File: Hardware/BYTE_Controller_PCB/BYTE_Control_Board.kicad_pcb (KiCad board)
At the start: 2 copper layers, 20.8 x 40.6 mm, 11 parts, among them J1 8P8C_Shielded, Q1 2N7002, U1 SeeeduinoXIAO

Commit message: modify controller board
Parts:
- removed C1: C, Capacitor_SMD:C_0603_1608Metric
- removed D1: D_Schottky, Diode_SMD:D_SOD-123
- removed Q1: 2N7002, Package_TO_SOT_SMD:SOT-23
- removed R1, R2, R3, R4, R5, R6: R_US, Resistor_SMD:R_0603_1608Metric_Pad1.05x0.95mm_HandSolder
- removed U1: SeeeduinoXIAO, XIAO:XIAO-MOUDLE14P-2.54-21X17.8MM_Through_Hole
- added REF**: U254051N4BH806, Connectors:U254051N4BH806, F.Cu at (172.2, 105.4)
- added REF**: BL653, Controller:BL653_v5, F.Cu at (160.3, 111.7)
- J1: moved to F.Cu
- moved J1 10.5 mm to (132.1, 105.8), turned to 270 degrees
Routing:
- net Net-(C1-Pad1): track 35.4 -> 0.00 mm
- net Net-(J1-Pad6): track 23.2 -> 0.00 mm
- net Net-(J1-Pad5): track 22.2 -> 0.00 mm
- net Net-(J1-Pad4): track 16.5 -> 0.00 mm
- net Net-(J1-Pad3): track 15.2 -> 0.00 mm
- net Net-(J1-Pad2): track 8.76 -> 0.00 mm
- net Net-(D1-Pad2): track 6.73 -> 0.00 mm
- net Net-(R6-Pad1): track 3.18 -> 0.00 mm
- net Net-(Q1-Pad1): track 1.84 -> 0.00 mm
- net GND: vias 5 -> 0
- removed copper zone on F.Cu, net (none)
- removed copper zone on B.Cu, net GND
- removed copper zone on F.Cu, net GND
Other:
- board size 20.8 x 40.6 mm -> 55 x 19.3 mm

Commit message: update pcbs
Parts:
- removed REF**: U254051N4BH806, Connectors:U254051N4BH806
- removed REF**: BL653, Controller:BL653_v5
- added C1: 4.7uF, Capacitor_SMD:C_0603_1608Metric, F.Cu at (145.6, 108.2)
- added C2: 4.7uF, Capacitor_SMD:C_0603_1608Metric, F.Cu at (147.6, 104.2)
- added D1: RED, LED_SMD:LED_0805_2012Metric, B.Cu at (122.0, 113.2)
- added D2: RED, LED_SMD:LED_0805_2012Metric, B.Cu at (121.9, 107.8)
- added P1: USB_C_Plug_USB2.0, Connectors:C393939, F.Cu at (168.5, 105.8)
- added R1: 2K, Resistor_SMD:R_0603_1608Metric, B.Cu at (125.4, 113.2)
- added R2: 2K, Resistor_SMD:R_0603_1608Metric, F.Cu at (149.6, 108.2)
- added R3: 2K, Resistor_SMD:R_0603_1608Metric, F.Cu at (141.4, 109.0)
- added R4: 2K, Resistor_SMD:R_0603_1608Metric, B.Cu at (125.2, 107.8)
- added R5: 2K, Resistor_SMD:R_0603_1608Metric, F.Cu at (139.9, 109.0)
- added U1: MCP73830T-2AAI_MYY, Controller:2x2TDFN, F.Cu at (147.6, 108.0)
- added U2: BL653, Controller:BL653_v5, F.Cu at (159.0, 112.0)
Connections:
- J1 pad 1: Net-(C1-Pad1) -> Net-(J1-Pad1)
- J1 pad 7: Net-(C1-Pad1) -> Net-(J1-Pad7)
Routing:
- net /STAT: track 0.00 -> 1.26 mm, vias 0 -> 1

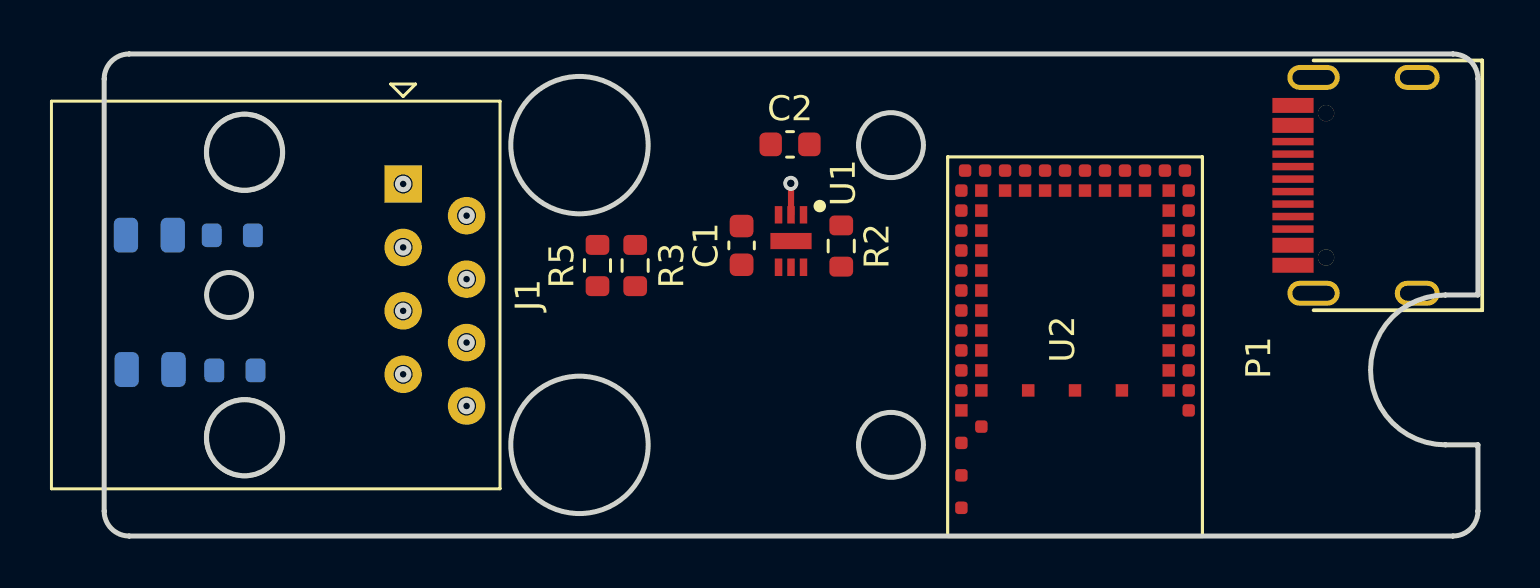
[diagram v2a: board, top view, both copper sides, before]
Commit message: update controller PCB added battery reading circuit
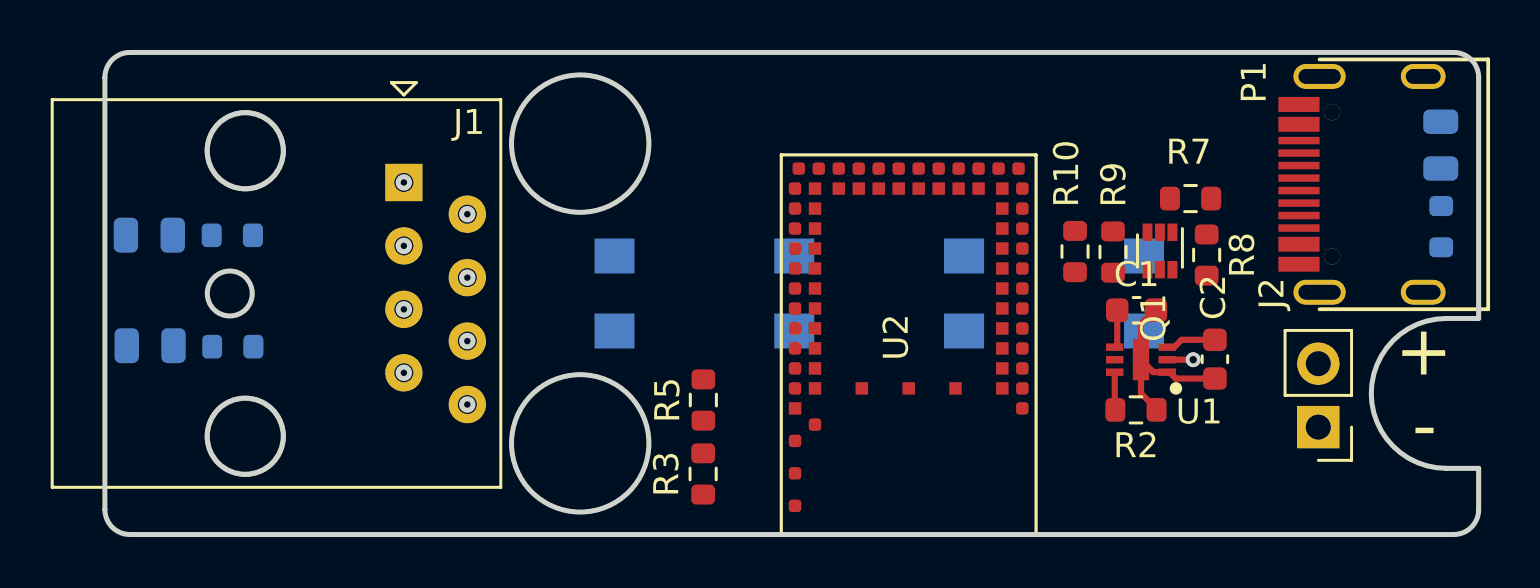
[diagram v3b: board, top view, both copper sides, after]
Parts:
- added D3: RED, LED_SMD:LED_0805_2012Metric, B.Cu at (122.0, 112.2)
- added J2: Battery, Connector_PinHeader_2.54mm:PinHeader_1x02_P2.54mm_Vertical, F.Cu at (168.7, 115.5)
- added Q1: DMC2400UV, Package_TO_SOT_SMD:SOT-563, F.Cu at (162.4, 108.5)
- added R10: 2K, Resistor_SMD:R_0603_1608Metric, F.Cu at (159.0, 108.5)
- added R6: 2K, Resistor_SMD:R_0603_1608Metric, B.Cu at (125.3, 112.3)
- added R7: 2K, Resistor_SMD:R_0603_1608Metric, F.Cu at (163.6, 106.3)
- added R8: 2K, Resistor_SMD:R_0603_1608Metric, F.Cu at (164.3, 108.6)
- added R9: 2K, Resistor_SMD:R_0603_1608Metric, F.Cu at (160.5, 108.5)
- added SW1: SW_Push, Button_Switch_SMD:SW_SPST_TL3305A, B.Cu at (144.2, 110.2)
- added SW2: SW_Push, Button_Switch_SMD:SW_SPST_TL3305A, B.Cu at (158.2, 110.2)
- moved D1 52.4 mm to (173.6, 104.2), turned to 90 degrees
- moved R1 48.6 mm to (173.7, 107.5), turned to 90 degrees
- moved C2 19.1 mm to (164.6, 112.8), turned to 270 degrees
- moved C1 16.0 mm to (161.5, 110.8), turned to 0 degrees
- moved U1 14.8 mm to (161.6, 112.8), turned to 180 degrees
- moved R2 13.5 mm to (161.4, 114.8), turned to 180 degrees
- moved R3 8.78 mm to (144.1, 117.4), turned to 270 degrees
- moved R5 6.85 mm to (144.1, 114.4)
- moved U2 6.66 mm to (152.3, 111.9)
- moved P1 0.24 mm to (168.8, 105.8)
- moved J1 0.07 mm to (132.1, 105.7)
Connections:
- R4 pad 1: /STAT -> /SIO_Z
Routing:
- net GND: track 0.00 -> 7.81 mm
- net +BATT: track 0.00 -> 2.03 mm
- net VBUS: track 0.00 -> 1.52 mm
- net Net-(R2-Pad2): track 0.00 -> 1.52 mm
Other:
- outline, holes or cut-outs redrawn
- board text added: "+"
- board text added: "-"

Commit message: update byte controller
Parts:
- added C3: 4.7uF, Capacitor_SMD:C_0603_1608Metric, F.Cu at (147.6, 103.7)
- added C4: 100nF, Capacitor_SMD:C_0603_1608Metric, F.Cu at (150.7, 103.7)
- added J3: Expansion, Connector_PinHeader_2.54mm:PinHeader_2x03_P2.54mm_Vertical, F.Cu at (138.2, 107.7)
- added J4: SWD, Connector_PinHeader_2.54mm:PinHeader_1x04_P2.54mm_Vertical, B.Cu at (127.2, 118.6)
- added R11: 5.1K, Resistor_SMD:R_0603_1608Metric, B.Cu at (170.5, 104.0)
- added R12: 5.1k, Resistor_SMD:R_0603_1608Metric, B.Cu at (171.9, 104.0)
- added R13: 10K, Resistor_SMD:R_0603_1608Metric, F.Cu at (145.6, 113.7)
- added REF**: OSHW-Logo2_7.3x6mm_SilkScreen, Symbol:OSHW-Logo2_7.3x6mm_SilkScreen, F.Cu at (143.7, 103.2)
- added Ref**: Val**, BYTE_Sensors:Logo, F.Cu at (155.5, 103.6)
- added SW3: RST, Button_Switch_SMD:SW_Push_1P1T-SH_NO_CK_KMR2xxG, F.Cu at (143.7, 117.6)
- SW1, SW2: value SW_Push -> GPIO
- moved D3 7.95 mm to (128.5, 107.7), turned to 0 degrees
- moved D2 7.88 mm to (128.5, 112.1), turned to 0 degrees
- moved R3 5.95 mm to (144.8, 111.5)
- moved R5 5.95 mm to (144.9, 108.5)
- moved R6 4.61 mm to (125.2, 107.7)
- moved R4 4.31 mm to (125.2, 112.1), turned to 0 degrees
- moved J2 0.57 mm to (169.2, 115.2)
- turned SW1 to 270 degrees
- turned SW2 to 270 degrees
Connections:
- J1 pad 2: Net-(J1-Pad2) -> /BYTE_SENSOR_1
- J1 pad 3: Net-(J1-Pad3) -> /SDA
- J1 pad 4: Net-(J1-Pad4) -> /SCL
- J1 pad 5: Net-(J1-Pad5) -> +BATT
- J1 pad 6: Net-(J1-Pad6) -> /Sensor_INT
- J1 pad 7: Net-(J1-Pad7) -> GND
- J1 pad 8: Net-(J1-Pad8) -> /BYTE_SENSOR_2
- Q1 pad 2: Net-(Q1-Pad2) -> /BATT_LVL_EN
- R10 pad 2: Net-(R10-Pad2) -> /BATT_LVL
- R4 pad 1: /SIO_Z -> /SIO_1
- R6 pad 1: /SIO_W -> /SIO_5
- R7 pad 2: Net-(Q1-Pad2) -> /BATT_LVL_EN
- R9 pad 1: Net-(R10-Pad2) -> /BATT_LVL
- SW1 pad 1: /SIO_X -> /SIO_20
- SW2 pad 1: /SIO_Y -> /SIO_0
- U2 pad 10: Net-(U2-Pad10) -> /SIO_24
- U2 pad 13: Net-(U2-Pad13) -> /SIO_20
- U2 pad 16: Net-(U2-Pad16) -> /BYTE_SENSOR_1
- U2 pad 18: Net-(U2-Pad18) -> /BYTE_SENSOR_2
- U2 pad 19: Net-(U2-Pad19) -> /RST
- U2 pad 24: Net-(U2-Pad24) -> VBUS
- U2 pad 25: Net-(U2-Pad25) -> +BATT
- U2 pad 37: Net-(U2-Pad37) -> /Sensor_INT
- U2 pad 39: Net-(U2-Pad39) -> /SIO_5
- U2 pad 41: Net-(U2-Pad41) -> /SIO_1
- U2 pad 42: Net-(U2-Pad42) -> /SIO_0
- U2 pad 45: Net-(U2-Pad45) -> /BATT_LVL_EN
- U2 pad 49: Net-(U2-Pad49) -> /BATT_LVL
- U2 pad 5: Net-(U2-Pad5) -> /SCL
- U2 pad 7: Net-(U2-Pad7) -> /SDA
- U2 pad 8: Net-(U2-Pad8) -> /SIO_25
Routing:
- net +BATT: track 2.03 -> 115.1 mm, vias 0 -> 3
- net VBUS: track 1.52 -> 62.5 mm, vias 0 -> 5
- net /SIO_1: track 0.00 -> 49.9 mm, vias 0 -> 1
- net GND: track 7.81 -> 55.4 mm, vias 0 -> 15
- net /Sensor_INT: track 0.00 -> 45.5 mm, vias 0 -> 2
- net /SIO_5: track 0.00 -> 42.8 mm, vias 0 -> 1
- net /BYTE_SENSOR_1: track 0.00 -> 39.2 mm, vias 0 -> 1
- net /D-: track 0.00 -> 38.1 mm
- net /D+: track 0.00 -> 38.1 mm
- net /BYTE_SENSOR_2: track 0.00 -> 35.8 mm, vias 0 -> 1
- net /SIO_25: track 0.00 -> 31.4 mm, vias 0 -> 1
- net /SIO_24: track 0.00 -> 30.7 mm, vias 0 -> 1
- net /SWCLK: track 0.00 -> 24.5 mm
- net /SWDIO: track 0.00 -> 22.8 mm
- net /RST: track 0.00 -> 19.4 mm, vias 0 -> 2
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- added copper zone on B.Cu, net GND
- added copper zone on F.Cu, net GND
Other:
- outline, holes or cut-outs redrawn
- net class Default: trace_width 0.25 -> 0.2
- board text added: "BYTE Controller"
- board text added: "CLK"
- board text added: "Controller"
- board text added: "DIO"
- board text added: "GND"
- board text added: "Vbatt"
- board text added: "v1.0"

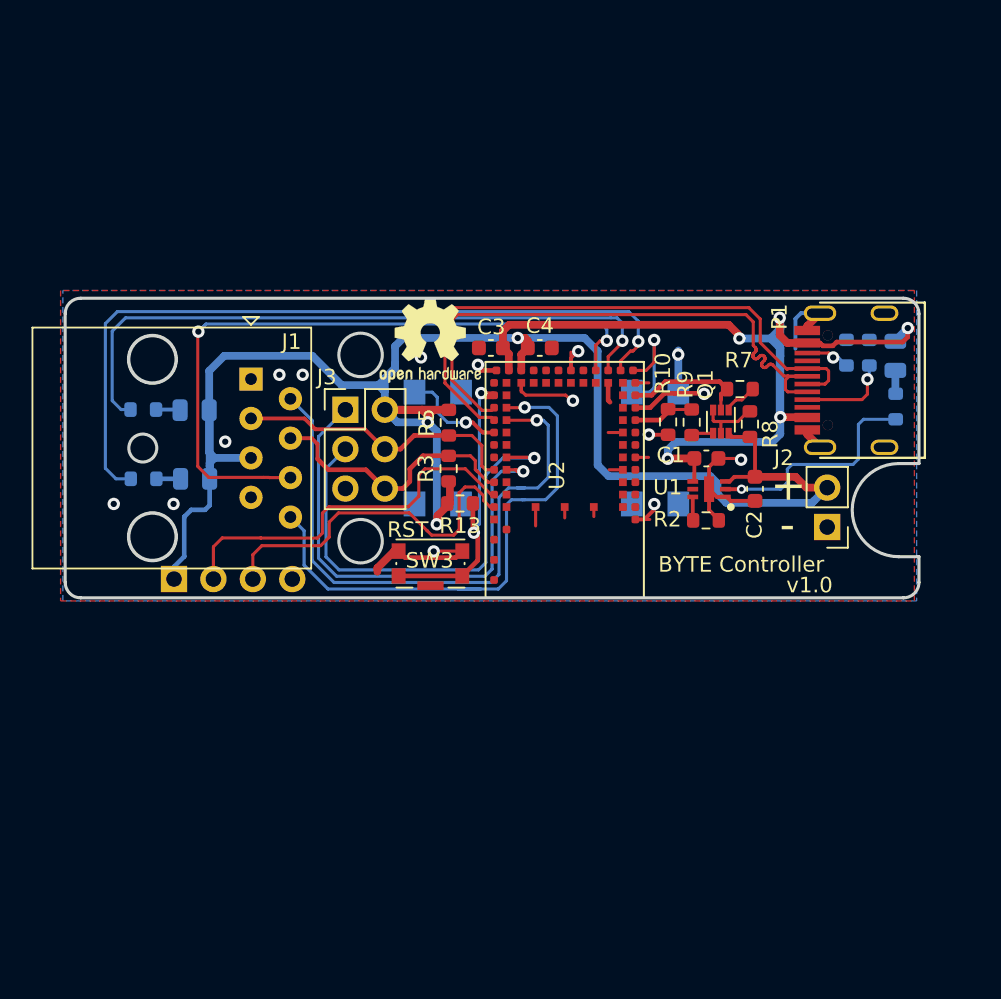
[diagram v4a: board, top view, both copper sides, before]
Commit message: update controller to v1.1
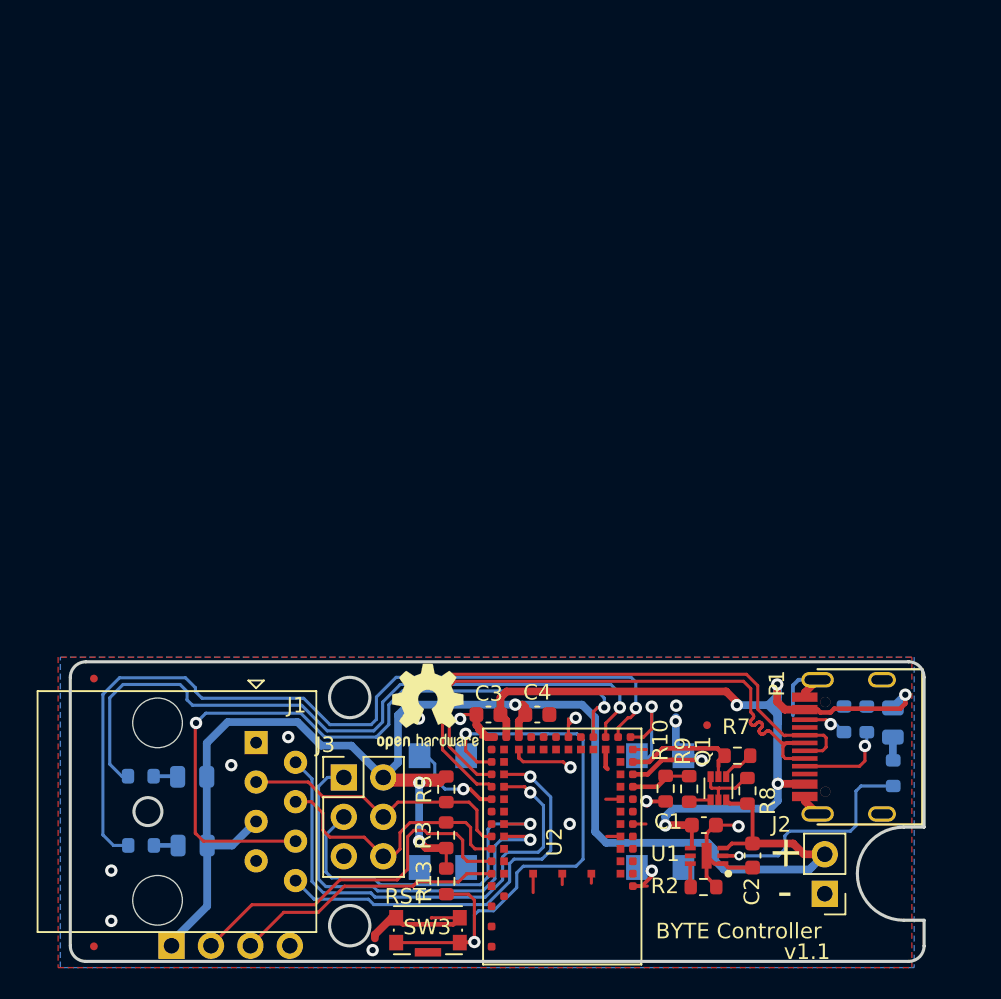
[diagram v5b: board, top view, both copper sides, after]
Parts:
- added REF**: Fiducial_0.5mm_Mask1mm, Fiducial:Fiducial_0.5mm_Mask1mm, F.Cu at (161.5, 128.0)
- added REF**: Fiducial_0.5mm_Mask1mm, Fiducial:Fiducial_0.5mm_Mask1mm, F.Cu at (122.0, 142.2)
- added REF**: Fiducial_0.5mm_Mask1mm, Fiducial:Fiducial_0.5mm_Mask1mm, F.Cu at (142.0, 125.0)
- added REF**: Fiducial_0.5mm_Mask1mm, Fiducial:Fiducial_0.5mm_Mask1mm, F.Cu at (122.0, 125.0)
- moved R13 24.4 mm to (144.7, 138.1), turned to 90 degrees
- moved J3 23.7 mm to (138.1, 131.4)
- moved D3 23.6 mm to (128.3, 131.3)
- moved J2 23.6 mm to (169.1, 138.9)
- moved R9 23.6 mm to (160.3, 132.1)
- moved C1 23.6 mm to (161.3, 134.4)
- moved C2 23.6 mm to (164.4, 136.4)
- moved D1 23.6 mm to (173.5, 127.8)
- moved J4 23.6 mm to (127.0, 142.2)
- moved P1 23.6 mm to (168.6, 129.4)
- moved R1 23.6 mm to (173.5, 131.1)
- moved R10 23.6 mm to (158.8, 132.1)
- moved R11 23.6 mm to (170.3, 127.6)
- moved R2 23.6 mm to (161.3, 138.4)
- moved R3 23.6 mm to (144.7, 135.1)
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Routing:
- net /RST: track 19.4 -> 40.1 mm
- net +BATT: track 115.1 -> 102.3 mm
- net /BYTE_SENSOR_2: track 35.8 -> 26.3 mm
- net /SIO_24: track 30.7 -> 22.7 mm
- net /BYTE_SENSOR_1: track 39.2 -> 31.4 mm
- net /SWDIO: track 22.8 -> 17.5 mm
- net /SIO_25: track 31.4 -> 27.1 mm
- net /SIO_1: track 49.9 -> 53.5 mm
- net GND: track 55.4 -> 58.9 mm, vias 15 -> 16
- net /SIO_5: track 42.8 -> 46.1 mm
- net /Sensor_INT: track 45.5 -> 46.3 mm
- net /SWCLK: track 24.5 -> 23.8 mm
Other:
- outline, holes or cut-outs redrawn
- board text added: "v1.1"
- board text removed: "v1.0"

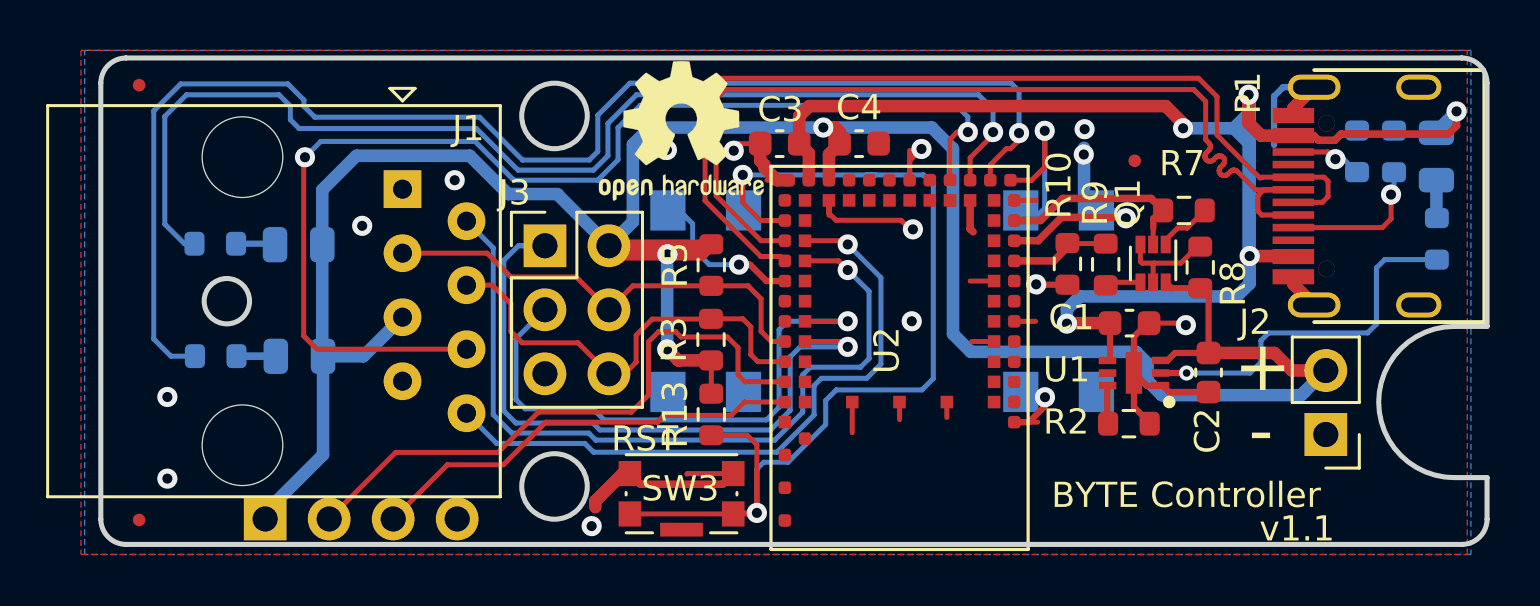
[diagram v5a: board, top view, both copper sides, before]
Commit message: update byte controller for hand made
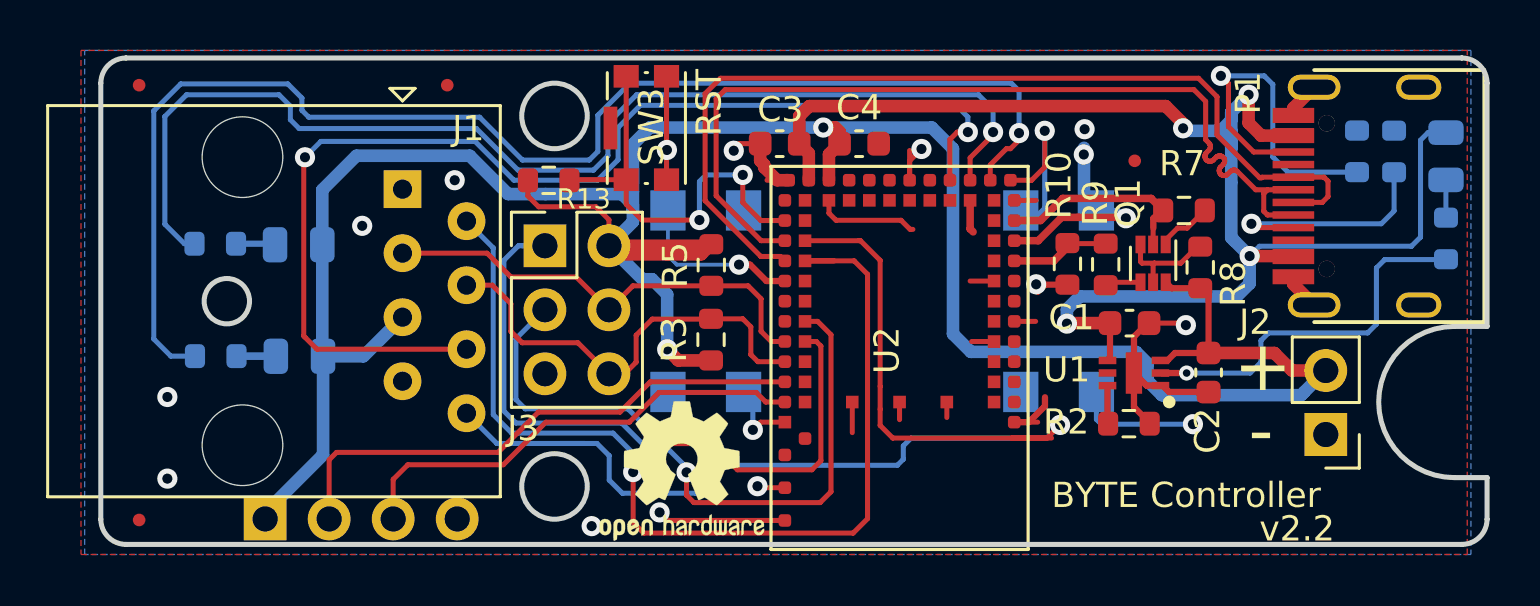
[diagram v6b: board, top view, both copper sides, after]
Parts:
- added REF**: Fiducial_0.5mm_Mask1mm, Fiducial:Fiducial_0.5mm_Mask1mm, F.Cu at (143.3, 138.2)
- moved SW3 14.6 mm to (142.1, 126.7), turned to 90 degrees
- moved REF** 13.5 mm to (143.5, 140.3)
- moved R13 11.3 mm to (138.2, 128.8), turned to 180 degrees
- moved REF** 7.78 mm to (134.2, 125.0)
- moved D1 0.38 mm to (173.8, 127.8)
- moved R1 0.36 mm to (173.8, 131.1)
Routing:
- net /RST: track 40.1 -> 16.9 mm
- net /BYTE_SENSOR_2: track 26.3 -> 46.8 mm
- net /CC2: track 2.86 -> 13.8 mm
- net /BYTE_SENSOR_1: track 31.4 -> 40.3 mm
- net +BATT: track 102.3 -> 109.9 mm, vias 3 -> 2
- net GND: track 58.9 -> 64.7 mm, vias 16 -> 17
- net /SIO_24: track 22.7 -> 26.5 mm
- net VBUS: track 62.5 -> 58.8 mm, vias 5 -> 4
- net /CC1: track 5.91 -> 9.13 mm
- net /SIO_25: track 27.1 -> 29.5 mm
- net /SWCLK: track 23.8 -> 21.7 mm
- net /D-: track 38.0 -> 36.5 mm
- net /SWDIO: track 17.5 -> 18.7 mm
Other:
- net class Default: clearance 0.2 -> 0.15
- rule trace_clearance: 0.2 -> 0.15
- rule trace_min: 0.2 -> 0.15
- board text added: "v2.2"
- board text removed: "v1.1"
